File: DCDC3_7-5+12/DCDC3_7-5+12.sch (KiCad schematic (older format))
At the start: 3 parts, among them T1 + 3.7V -, T2 + 12V -, T3 + 5V -

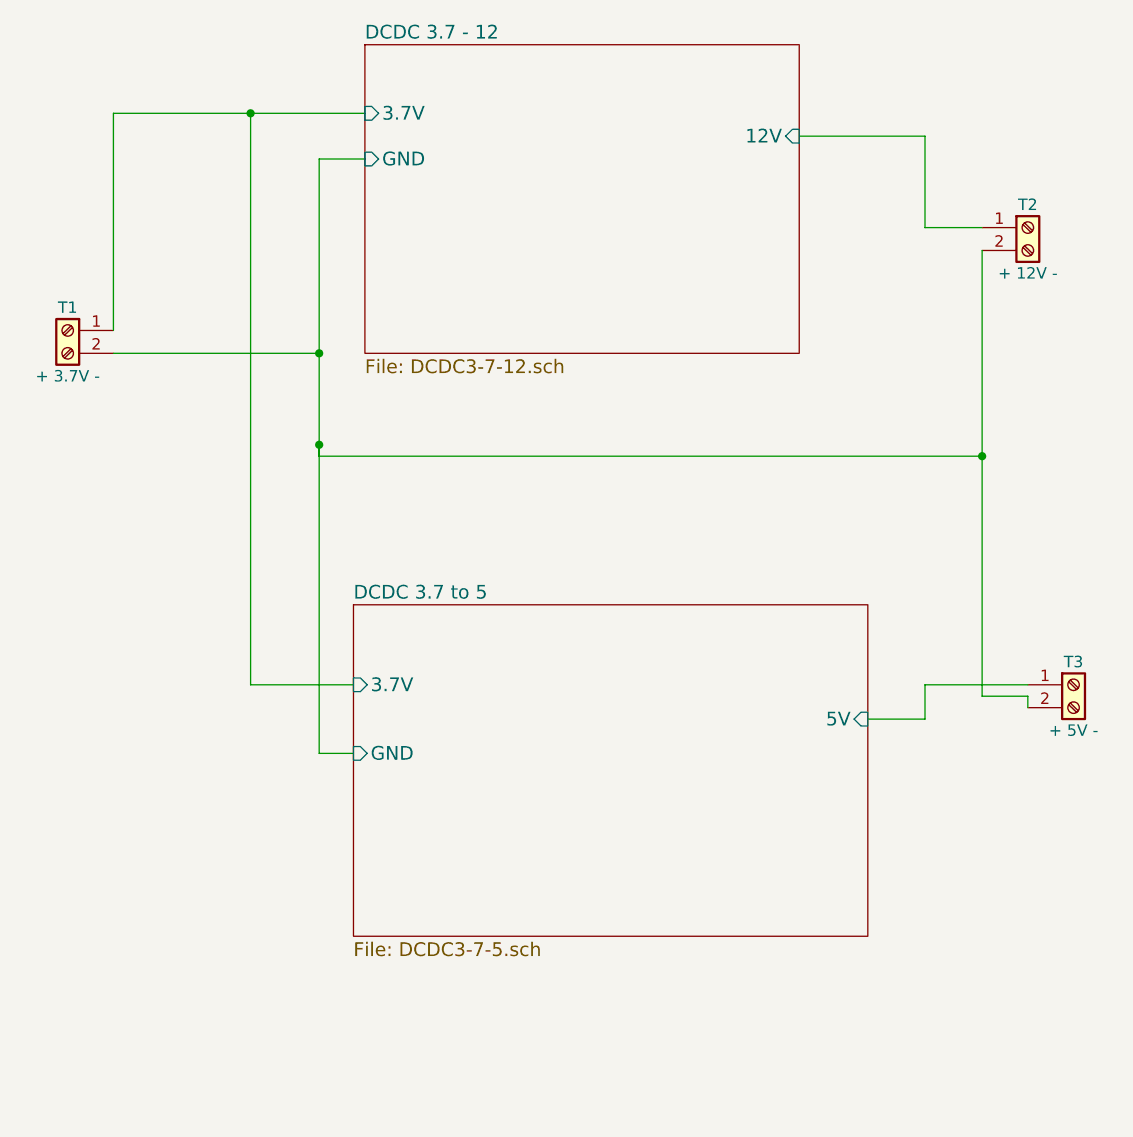
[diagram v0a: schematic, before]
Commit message: Add mounting holes, adjust things to accomadate mounting holes.
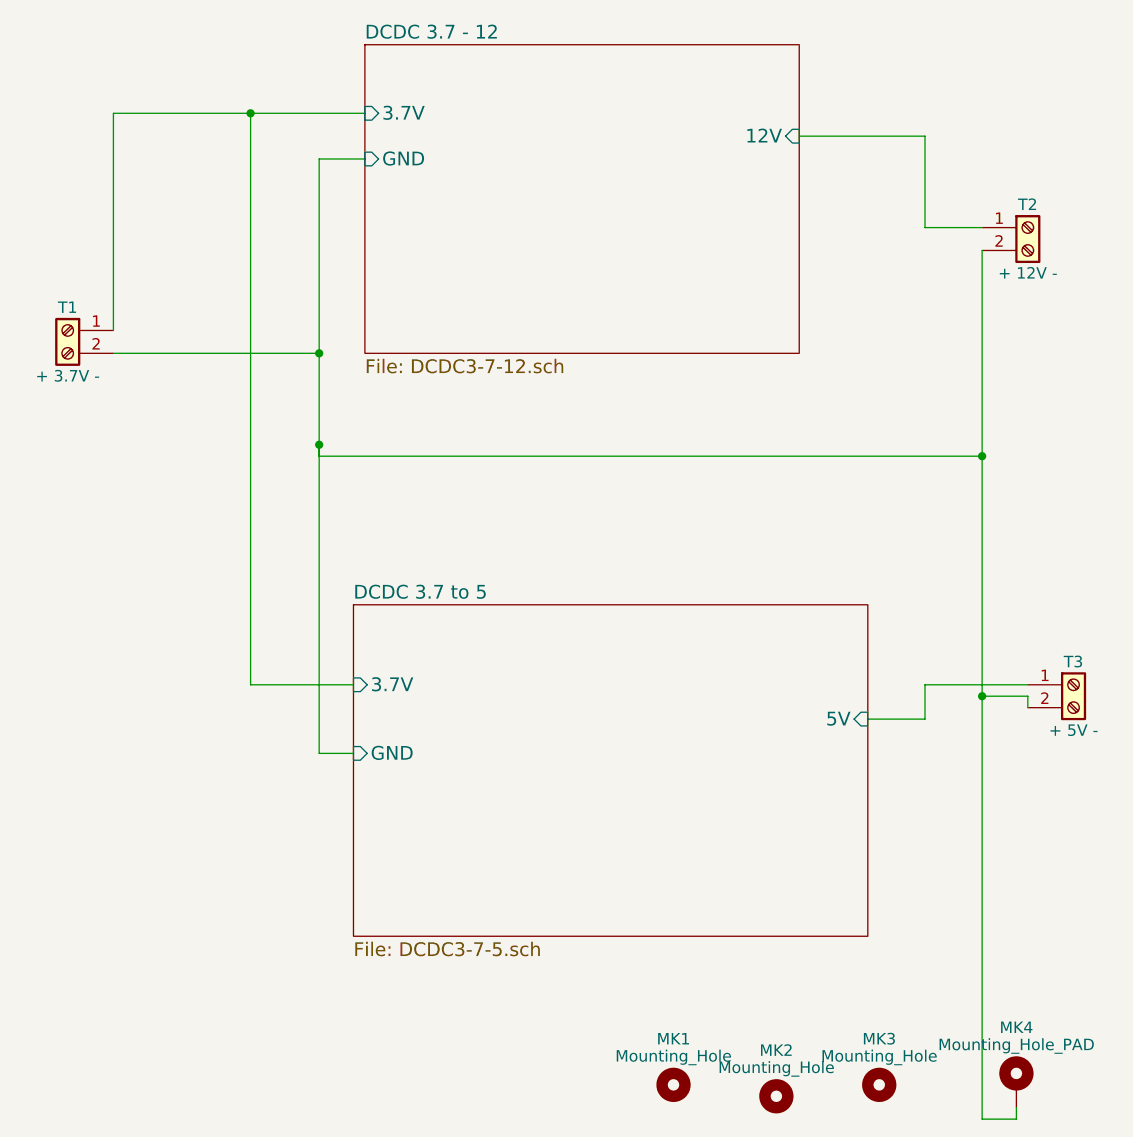
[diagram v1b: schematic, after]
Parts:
- added MK1, MK2, MK3: Mounting_Hole, Mounting_Holes:MountingHole_3.5mm, symbol Mounting_Hole
- added MK4: Mounting_Hole_PAD, Mounting_Holes:MountingHole_3.5mm_Pad, symbol Mounting_Hole_PAD
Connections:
- net DCDC 3.7 - 12/GND: now also MK4.1
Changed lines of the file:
@@
 LIBS:valves
 LIBS:xl6009
+LIBS:mechanical
 LIBS:DCDC3_7-5+12-cache
 EELAYER 25 0
@@
 	5150 4950 5600 4950
 Wire Wire Line
-	5400 3050 5400 5000
+	5400 3050 5400 6850
 Wire Wire Line
 	5400 5000 5600 5000
@@
 Connection ~ 2500 3900
 Connection ~ 5400 3950
+$Comp
+L Mounting_Hole MK1
+U 1 1 62AB236D
+P 4050 6700
+F 0 "MK1" H 4050 6900 50  0000 C CNN
+F 1 "Mounting_Hole" H 4050 6825 50  0000 C CNN
+F 2 "Mounting_Holes:MountingHole_3.5mm" H 4050 6700 50  0001 C CNN
+F 3 "" H 4050 6700 50  0001 C CNN
+	1    4050 6700
+	1    0    0    -1
+$EndComp
+$Comp
+L Mounting_Hole MK2
+U 1 1 62AB23F8
+P 4500 6750
+F 0 "MK2" H 4500 6950 50  0000 C CNN
+F 1 "Mounting_Hole" H 4500 6875 50  0000 C CNN
+F 2 "Mounting_Holes:MountingHole_3.5mm" H 4500 6750 50  0001 C CNN
+F 3 "" H 4500 6750 50  0001 C CNN
+	1    4500 6750
+	1    0    0    -1
+$EndComp
+$Comp
+L Mounting_Hole MK3
+U 1 1 62AB2447
+P 4950 6700
+F 0 "MK3" H 4950 6900 50  0000 C CNN
+F 1 "Mounting_Hole" H 4950 6825 50  0000 C CNN
+F 2 "Mounting_Holes:MountingHole_3.5mm" H 4950 6700 50  0001 C CNN
+F 3 "" H 4950 6700 50  0001 C CNN
+	1    4950 6700
+	1    0    0    -1
+$EndComp
+$Comp
+L Mounting_Hole_PAD MK4
+U 1 1 62AB248C
+P 5550 6700
+F 0 "MK4" H 5550 6950 50  0000 C CNN
+F 1 "Mounting_Hole_PAD" H 5550 6875 50  0000 C CNN
+F 2 "Mounting_Holes:MountingHole_3.5mm_Pad" H 5550 6700 50  0001 C CNN
+F 3 "" H 5550 6700 50  0001 C CNN
+	1    5550 6700
+	1    0    0    -1
+$EndComp
+Wire Wire Line
+	5400 6850 5550 6850
+Wire Wire Line
+	5550 6850 5550 6800
+Connection ~ 5400 5000
 $EndSCHEMATC

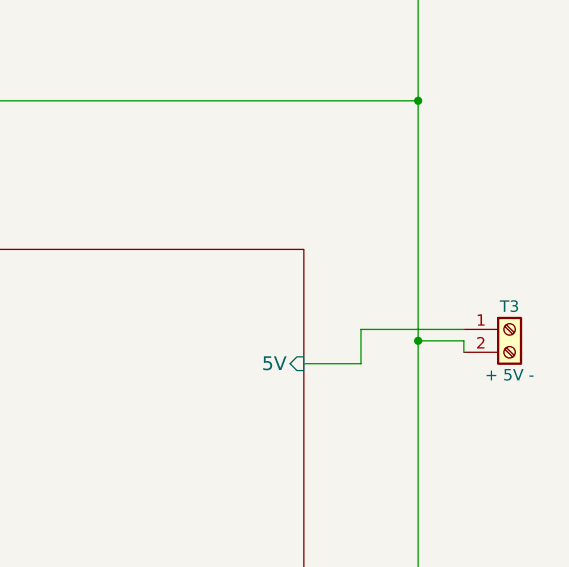
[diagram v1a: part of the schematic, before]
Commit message: Add FAN header, minor trace updates.
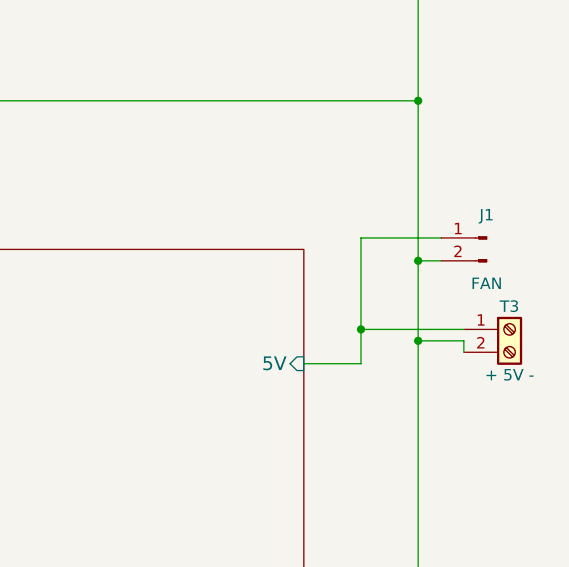
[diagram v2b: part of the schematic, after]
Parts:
- added J1: FAN, Pin_Headers:Pin_Header_Straight_1x02_Pitch2.54mm, symbol Conn_01x02_Male
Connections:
- net DCDC 3.7 - 12/GND: now also J1.2 (Pin_2)
- net DCDC 3.7 to 5/5V: now also J1.1 (Pin_1)
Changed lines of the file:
@@
 	5150 2950 5400 2950
 Wire Wire Line
-	4900 5100 5150 5100
+	5150 5100 4900 5100
 Wire Wire Line
-	5150 5100 5150 4950
+	5150 4550 5150 5100
 Wire Wire Line
 	5150 4950 5600 4950
@@
 	5550 6850 5550 6800
 Connection ~ 5400 5000
+$Comp
+L Conn_01x02_Male J1
+U 1 1 62AB8A27
+P 5700 4550
+F 0 "J1" H 5700 4650 50  0000 C CNN
+F 1 "FAN" H 5700 4350 50  0000 C CNN
+F 2 "Pin_Headers:Pin_Header_Straight_1x02_Pitch2.54mm" H 5700 4550 50  0001 C CNN
+F 3 "" H 5700 4550 50  0001 C CNN
+	1    5700 4550
+	-1   0    0    -1
+$EndComp
+Wire Wire Line
+	5500 4650 5400 4650
+Connection ~ 5400 4650
+Wire Wire Line
+	5500 4550 5150 4550
+Connection ~ 5150 4950
 $EndSCHEMATC
